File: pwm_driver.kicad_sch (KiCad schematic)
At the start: 147 parts, among them J11 POWER, Q1 Si7450DP, Q10 Si7450DP, Q11 Si7450DP, Q12 Si7450DP, Q13 Si7450DP, Q14 Si7450DP, Q15 Si7450DP, Q16 Si7450DP, Q2 Si7450DP, Q3 Si7450DP, Q4 Si7450DP, Q5 Si7450DP, Q6 Si7450DP, Q7 Si7450DP, Q8 Si7450DP, Q9 Si7450DP

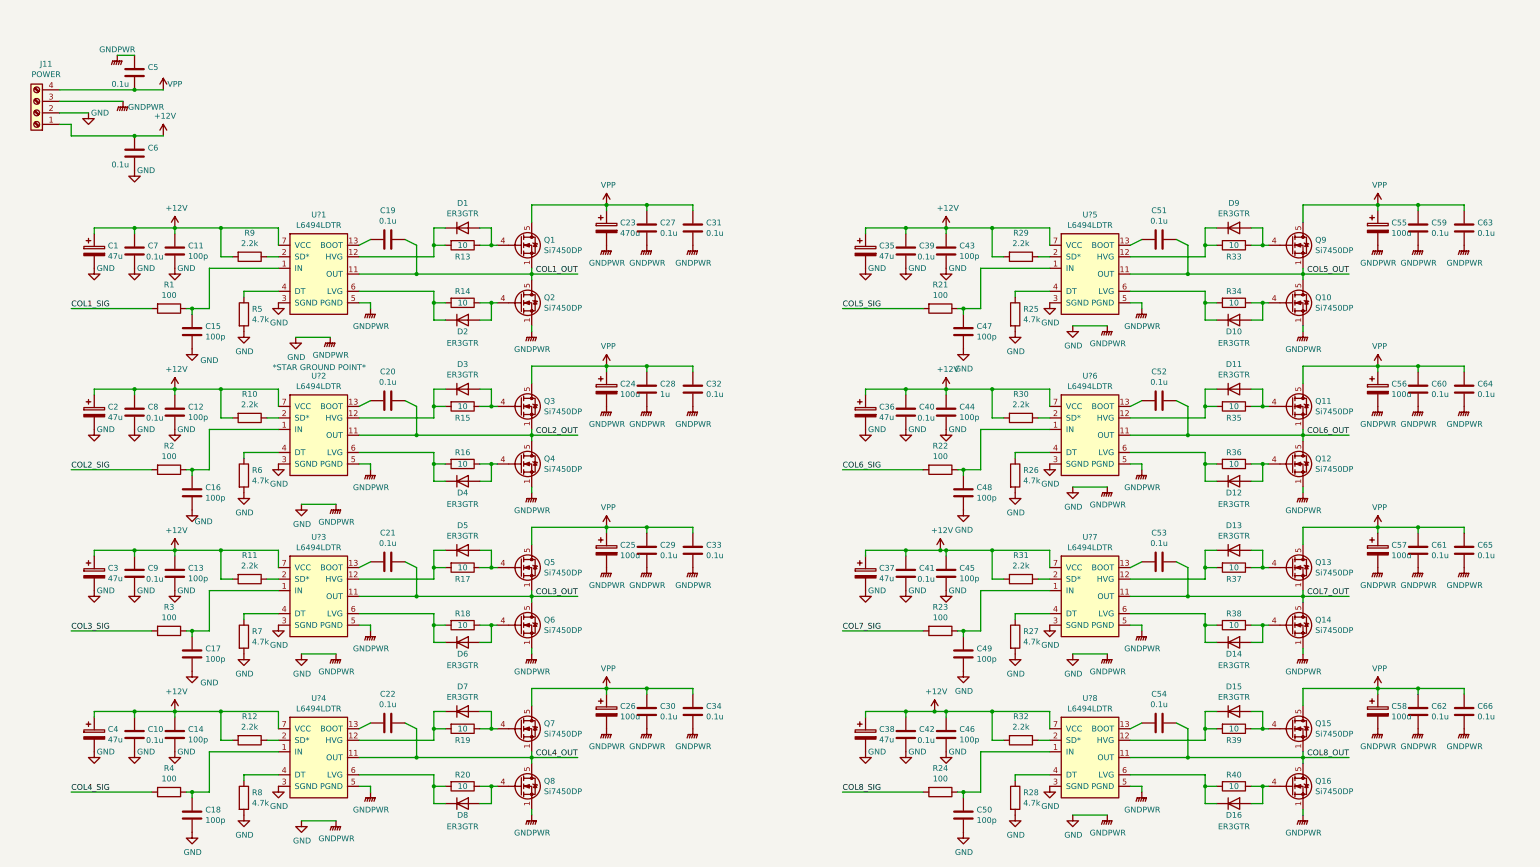
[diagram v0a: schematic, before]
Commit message: trace widths in amplifier channel adjusted
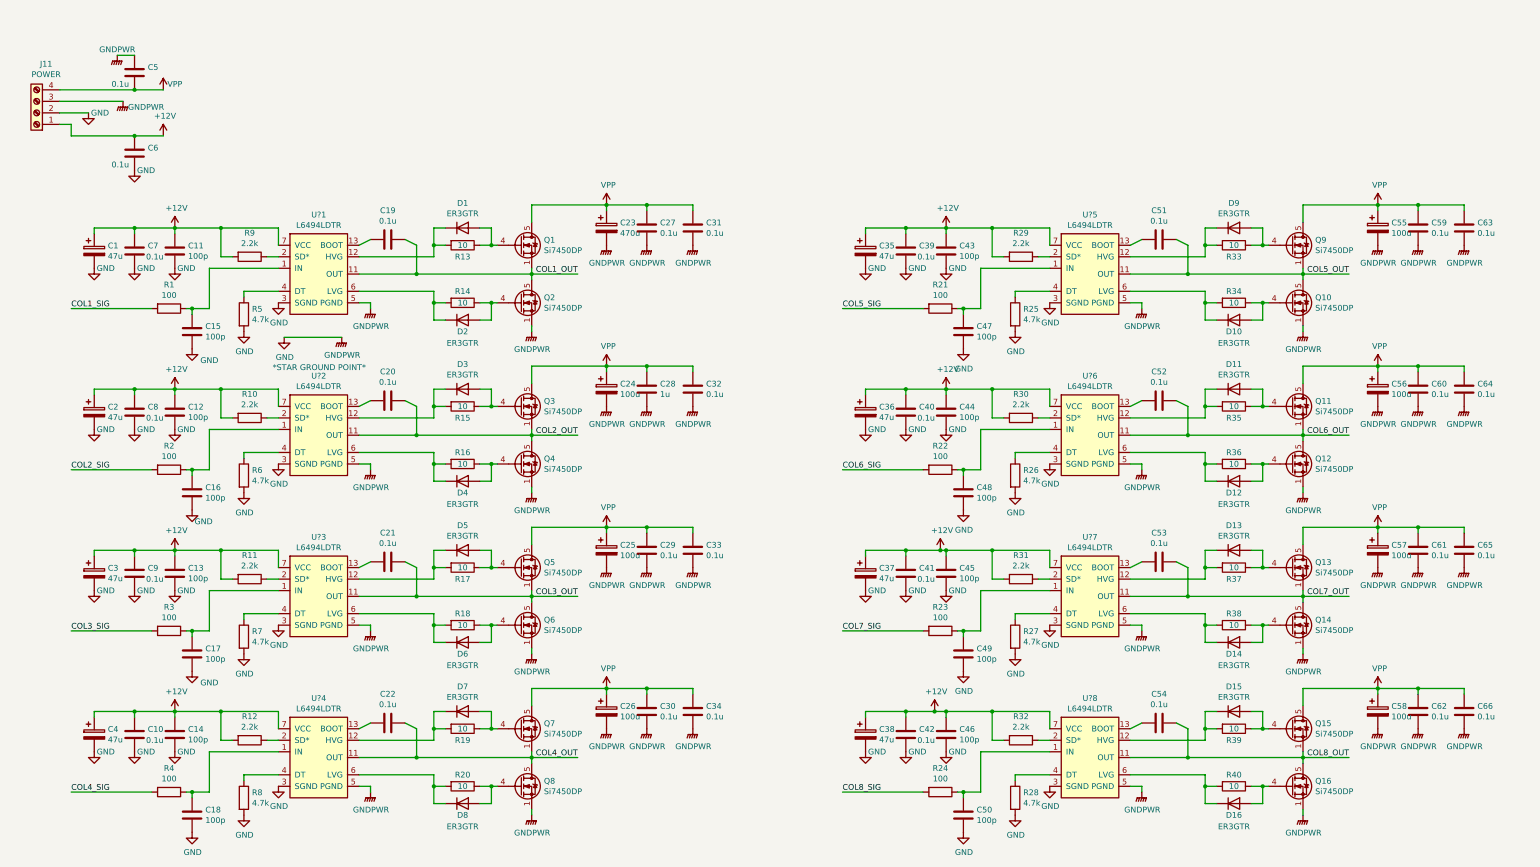
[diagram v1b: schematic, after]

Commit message: all major components added, routing underway
added and fixed some component footprints. routed column signals and designed/layout of audio amplifier and power supply. NEED TO CHECK CAP VOLTAGES
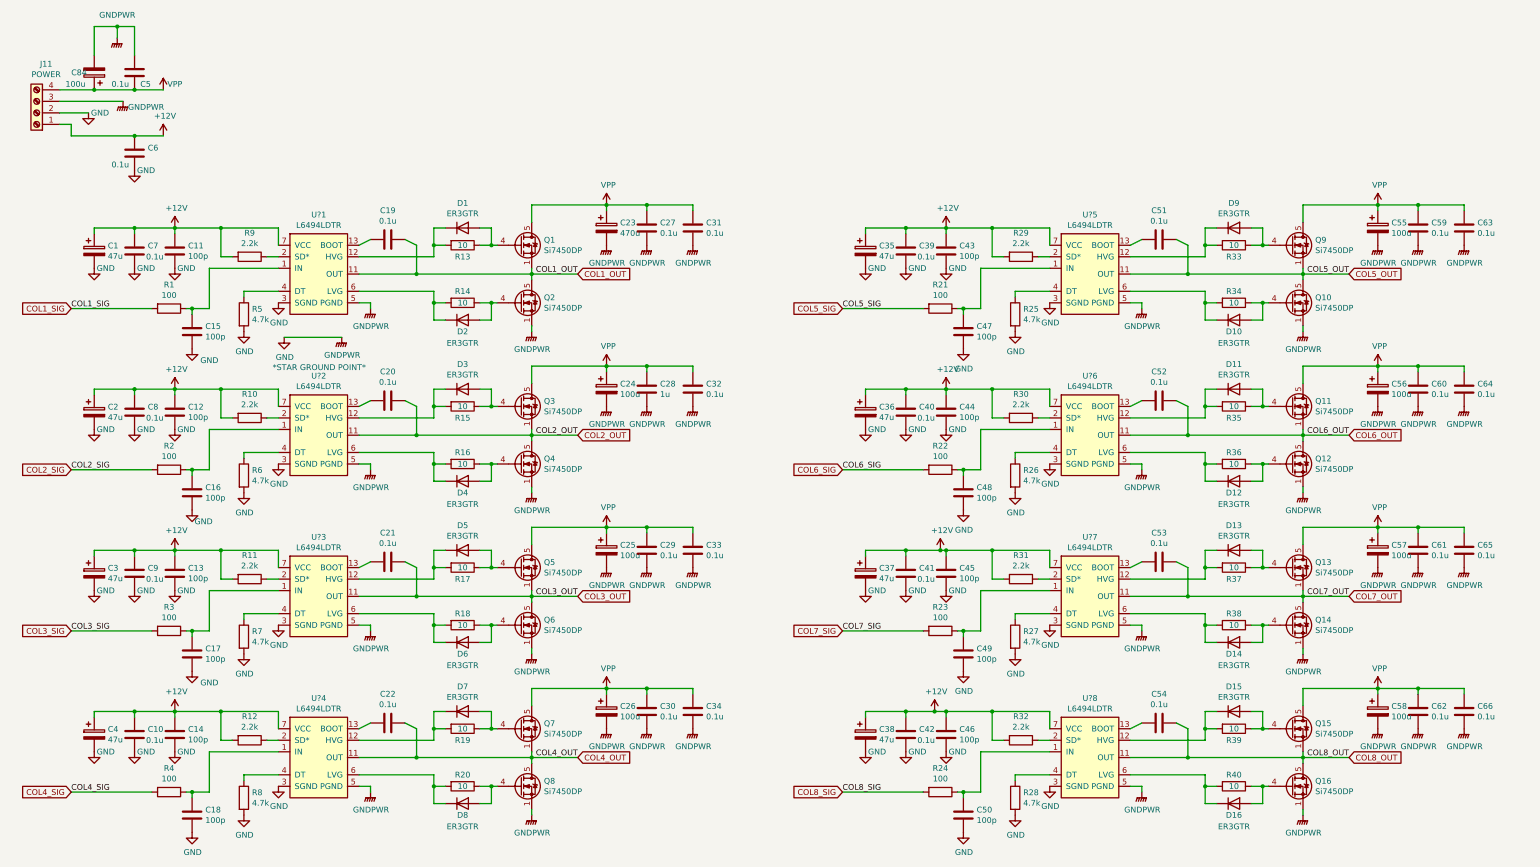
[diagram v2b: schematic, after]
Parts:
- added C84: 100u, Capacitor_THT:CP_Radial_D18.0mm_P7.50mm, symbol Device:C_Polarized
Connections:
- net GND: now also C84.2
- net VPP: now also C84.1
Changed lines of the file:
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@@
   (junction (at 313.69 88.9) (diameter 0) (color 0 0 0 0)
   )
+  (junction (at 55.88 41.91) (diameter 0) (color 0 0 0 0)
+  )
   (junction (at 322.58 118.11) (diameter 0) (color 0 0 0 0)
   )
@@
   (junction (at 300.99 124.46) (diameter 0) (color 0 0 0 0)
   )
+  (junction (at 60.96 27.94) (diameter 0) (color 0 0 0 0)
+  )
   (junction (at 127 189.23) (diameter 0) (color 0 0 0 0)
   )
@@
     (stroke (width 0) (type default) (color 0 0 0 0))
   )
+  (wire (pts (xy 55.88 34.29) (xy 55.88 27.94))
+    (stroke (width 0) (type default) (color 0 0 0 0))
+  )
   (wire (pts (xy 152.4 173.99) (xy 168.91 173.99))
     (stroke (width 0) (type default) (color 0 0 0 0))
@@
     (stroke (width 0) (type default) (color 0 0 0 0))
   )
+  (wire (pts (xy 55.88 41.91) (xy 64.77 41.91))
+    (stroke (width 0) (type default) (color 0 0 0 0))
+  )
   (wire (pts (xy 254 143.51) (xy 266.7 143.51))
     (stroke (width 0) (type default) (color 0 0 0 0))
@@
     (stroke (width 0) (type default) (color 0 0 0 0))
   )
-  (wire (pts (xy 48.26 41.91) (xy 64.77 41.91))
+  (wire (pts (xy 48.26 41.91) (xy 55.88 41.91))
     (stroke (width 0) (type default) (color 0 0 0 0))
   )
@@
     (stroke (width 0) (type default) (color 0 0 0 0))
   )
-  (wire (pts (xy 60.96 34.29) (xy 64.77 34.29))
+  (wire (pts (xy 60.96 27.94) (xy 64.77 27.94))
     (stroke (width 0) (type default) (color 0 0 0 0))
   )
@@
     (stroke (width 0) (type default) (color 0 0 0 0))
   )
+  (wire (pts (xy 60.96 27.94) (xy 60.96 30.48))
+    (stroke (width 0) (type default) (color 0 0 0 0))
+  )
   (wire (pts (xy 130.81 195.58) (xy 130.81 199.39))
     (stroke (width 0) (type default) (color 0 0 0 0))
@@
     (stroke (width 0) (type default) (color 0 0 0 0))
   )
+  (wire (pts (xy 55.88 27.94) (xy 60.96 27.94))
+    (stroke (width 0) (type default) (color 0 0 0 0))
+  )
   (wire (pts (xy 313.69 182.88) (xy 311.15 182.88))
     (stroke (width 0) (type default) (color 0 0 0 0))
@@
     (stroke (width 0) (type default) (color 0 0 0 0))
   )
+  (wire (pts (xy 64.77 27.94) (xy 64.77 34.29))
+    (stroke (width 0) (type default) (color 0 0 0 0))
+  )
   (wire (pts (xy 322.58 102.87) (xy 339.09 102.87))
     (stroke (width 0) (type default) (color 0 0 0 0))
@@
     (effects (font (size 1.27 1.27)) (justify right bottom))
   )
+  (global_label "COL8_SIG" (shape input) (at 220.98 196.85 180) (fields_autoplaced)
+    (effects (font (size 1.27 1.27)) (justify right))
+    (property "Intersheet References" "${INTERSHEET_REFS}" (id 0) (at 209.7658 196.7706 0)
+      (effects (font (size 1.27 1.27)) (justify right) hide)
+    )
+  )
+  (global_label "COL4_SIG" (shape input) (at 50.8 196.85 180) (fields_autoplaced)
+    (effects (font (size 1.27 1.27)) (justify right))
+    (property "Intersheet References" "${INTERSHEET_REFS}" (id 0) (at 39.5858 196.7706 0)
+      (effects (font (size 1.27 1.27)) (justify right) hide)
+    )
+  )
+  (global_label "COL2_SIG" (shape input) (at 50.8 125.73 180) (fields_autoplaced)
+    (effects (font (size 1.27 1.27)) (justify right))
+    (property "Intersheet References" "${INTERSHEET_REFS}" (id 0) (at 39.5858 125.6506 0)
+      (effects (font (size 1.27 1.27)) (justify right) hide)
+    )
+  )
+  (global_label "COL1_SIG" (shape input) (at 50.8 90.17 180) (fields_autoplaced)
+    (effects (font (size 1.27 1.27)) (justify right))
+    (property "Intersheet References" "${INTERSHEET_REFS}" (id 0) (at 39.5858 90.0906 0)
+      (effects (font (size 1.27 1.27)) (justify right) hide)
+    )
+  )
+  (global_label "COL2_OUT" (shape input) (at 162.56 118.11 0) (fields_autoplaced)
+    (effects (font (size 1.27 1.27)) (justify left))
+    (property "Intersheet References" "${INTERSHEET_REFS}" (id 0) (at 174.3185 118.0306 0)
+      (effects (font (size 1.27 1.27)) (justify left) hide)
+    )
+  )
+  (global_label "COL8_OUT" (shape input) (at 332.74 189.23 0) (fields_autoplaced)
+    (effects (font (size 1.27 1.27)) (justify left))
+    (property "Intersheet References" "${INTERSHEET_REFS}" (id 0) (at 344.4985 189.1506 0)
+      (effects (font (size 1.27 1.27)) (justify left) hide)
+    )
+  )
+  (global_label "COL7_OUT" (shape input) (at 332.74 153.67 0) (fields_autoplaced)
+    (effects (font (size 1.27 1.27)) (justify left))
+    (property "Intersheet References" "${INTERSHEET_REFS}" (id 0) (at 344.4985 153.5906 0)
+      (effects (font (size 1.27 1.27)) (justify left) hide)
+    )
+  )
+  (global_label "COL1_OUT" (shape input) (at 162.56 82.55 0) (fields_autoplaced)
+    (effects (font (size 1.27 1.27)) (justify left))
+    (property "Intersheet References" "${INTERSHEET_REFS}" (id 0) (at 174.3185 82.4706 0)
+      (effects (font (size 1.27 1.27)) (justify left) hide)
+    )
+  )
+  (global_label "COL3_SIG" (shape input) (at 50.8 161.29 180) (fields_autoplaced)
+    (effects (font (size 1.27 1.27)) (justify right))
+    (property "Intersheet References" "${INTERSHEET_REFS}" (id 0) (at 39.5858 161.2106 0)
+      (effects (font (size 1.27 1.27)) (justify right) hide)
+    )
+  )
+  (global_label "COL3_OUT" (shape input) (at 162.56 153.67 0) (fields_autoplaced)
+    (effects (font (size 1.27 1.27)) (justify left))
+    (property "Intersheet References" "${INTERSHEET_REFS}" (id 0) (at 174.3185 153.5906 0)
+      (effects (font (size 1.27 1.27)) (justify left) hide)
+    )
+  )
+  (global_label "COL6_OUT" (shape input) (at 332.74 118.11 0) (fields_autoplaced)
+    (effects (font (size 1.27 1.27)) (justify left))
+    (property "Intersheet References" "${INTERSHEET_REFS}" (id 0) (at 344.4985 118.0306 0)
+      (effects (font (size 1.27 1.27)) (justify left) hide)
+    )
+  )
+  (global_label "COL5_OUT" (shape input) (at 332.74 82.55 0) (fields_autoplaced)
+    (effects (font (size 1.27 1.27)) (justify left))
+    (property "Intersheet References" "${INTERSHEET_REFS}" (id 0) (at 344.4985 82.4706 0)
+      (effects (font (size 1.27 1.27)) (justify left) hide)
+    )
+  )
+  (global_label "COL6_SIG" (shape input) (at 220.98 125.73 180) (fields_autoplaced)
+    (effects (font (size 1.27 1.27)) (justify right))
+    (property "Intersheet References" "${INTERSHEET_REFS}" (id 0) (at 209.7658 125.6506 0)
+      (effects (font (size 1.27 1.27)) (justify right) hide)
+    )
+  )
+  (global_label "COL4_OUT" (shape input) (at 162.56 189.23 0) (fields_autoplaced)
+    (effects (font (size 1.27 1.27)) (justify left))
+    (property "Intersheet References" "${INTERSHEET_REFS}" (id 0) (at 174.3185 189.1506 0)
+      (effects (font (size 1.27 1.27)) (justify left) hide)
+    )
+  )
+  (global_label "COL5_SIG" (shape input) (at 220.98 90.17 180) (fields_autoplaced)
+    (effects (font (size 1.27 1.27)) (justify right))
+    (property "Intersheet References" "${INTERSHEET_REFS}" (id 0) (at 209.7658 90.0906 0)
+      (effects (font (size 1.27 1.27)) (justify right) hide)
+    )
+  )
+  (global_label "COL7_SIG" (shape input) (at 220.98 161.29 180) (fields_autoplaced)
+    (effects (font (size 1.27 1.27)) (justify right))
+    (property "Intersheet References" "${INTERSHEET_REFS}" (id 0) (at 209.7658 161.2106 0)
+      (effects (font (size 1.27 1.27)) (justify right) hide)
+    )
+  )
   (symbol (lib_id "Device:C") (at 120.65 74.93 270) (unit 1)
     (in_bom yes) (on_board yes)
@@
   (symbol (lib_id "Device:C") (at 64.77 38.1 0) (unit 1)
     (in_bom yes) (on_board yes)
-    (property "Reference" "C5" (id 0) (at 67.691 36.9316 0)
+    (property "Reference" "C5" (id 0) (at 66.04 40.64 0)
       (effects (font (size 1.27 1.27)) (justify left))
     )
@@
     (pin "2")
   )
-  (symbol (lib_id "power:GNDPWR") (at 60.96 34.29 0) (unit 1)
+  (symbol (lib_id "power:GNDPWR") (at 60.96 30.48 0) (unit 1)
     (in_bom yes) (on_board yes)
-    (property "Reference" "#PWR0235" (id 0) (at 60.96 39.37 0)
+    (property "Reference" "#PWR0235" (id 0) (at 60.96 35.56 0)
       (effects (font (size 1.27 1.27)) hide)
     )
-    (property "Value" "GNDPWR" (id 1) (at 60.96 33.02 0))
-    (property "Footprint" "" (id 2) (at 60.96 35.56 0)
+    (property "Value" "GNDPWR" (id 1) (at 60.96 25.4 0))
+    (property "Footprint" "" (id 2) (at 60.96 31.75 0)
       (effects (font (size 1.27 1.27)) hide)
     )
-    (property "Datasheet" "" (id 3) (at 60.96 35.56 0)
+    (property "Datasheet" "" (id 3) (at 60.96 31.75 0)
       (effects (font (size 1.27 1.27)) hide)
     )
@@
     (pin "1")
   )
+  (symbol (lib_id "Device:C_Polarized") (at 55.88 38.1 180) (unit 1)
+    (in_bom yes) (on_board yes)
+    (property "Reference" "C84" (id 0) (at 50.8 38.1 0)
+      (effects (font (size 1.27 1.27)) (justify right))
+    )
+    (property "Value" "100u" (id 1) (at 49.53 40.64 0)
+      (effects (font (size 1.27 1.27)) (justify right))
+    )
+    (property "Footprint" "Capacitor_THT:CP_Radial_D18.0mm_P7.50mm" (id 2) (at 54.9148 34.29 0)
+      (effects (font (size 1.27 1.27)) hide)
+    )
+    (property "Datasheet" "~" (id 3) (at 55.88 38.1 0)
+      (effects (font (size 1.27 1.27)) hide)
+    )
+    (pin "1")
+    (pin "2")
+  )
 )
